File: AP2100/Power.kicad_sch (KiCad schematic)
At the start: 35 parts, among them U2 MPQ8634AGLE-P, U3 MPQ8634AGLE-P

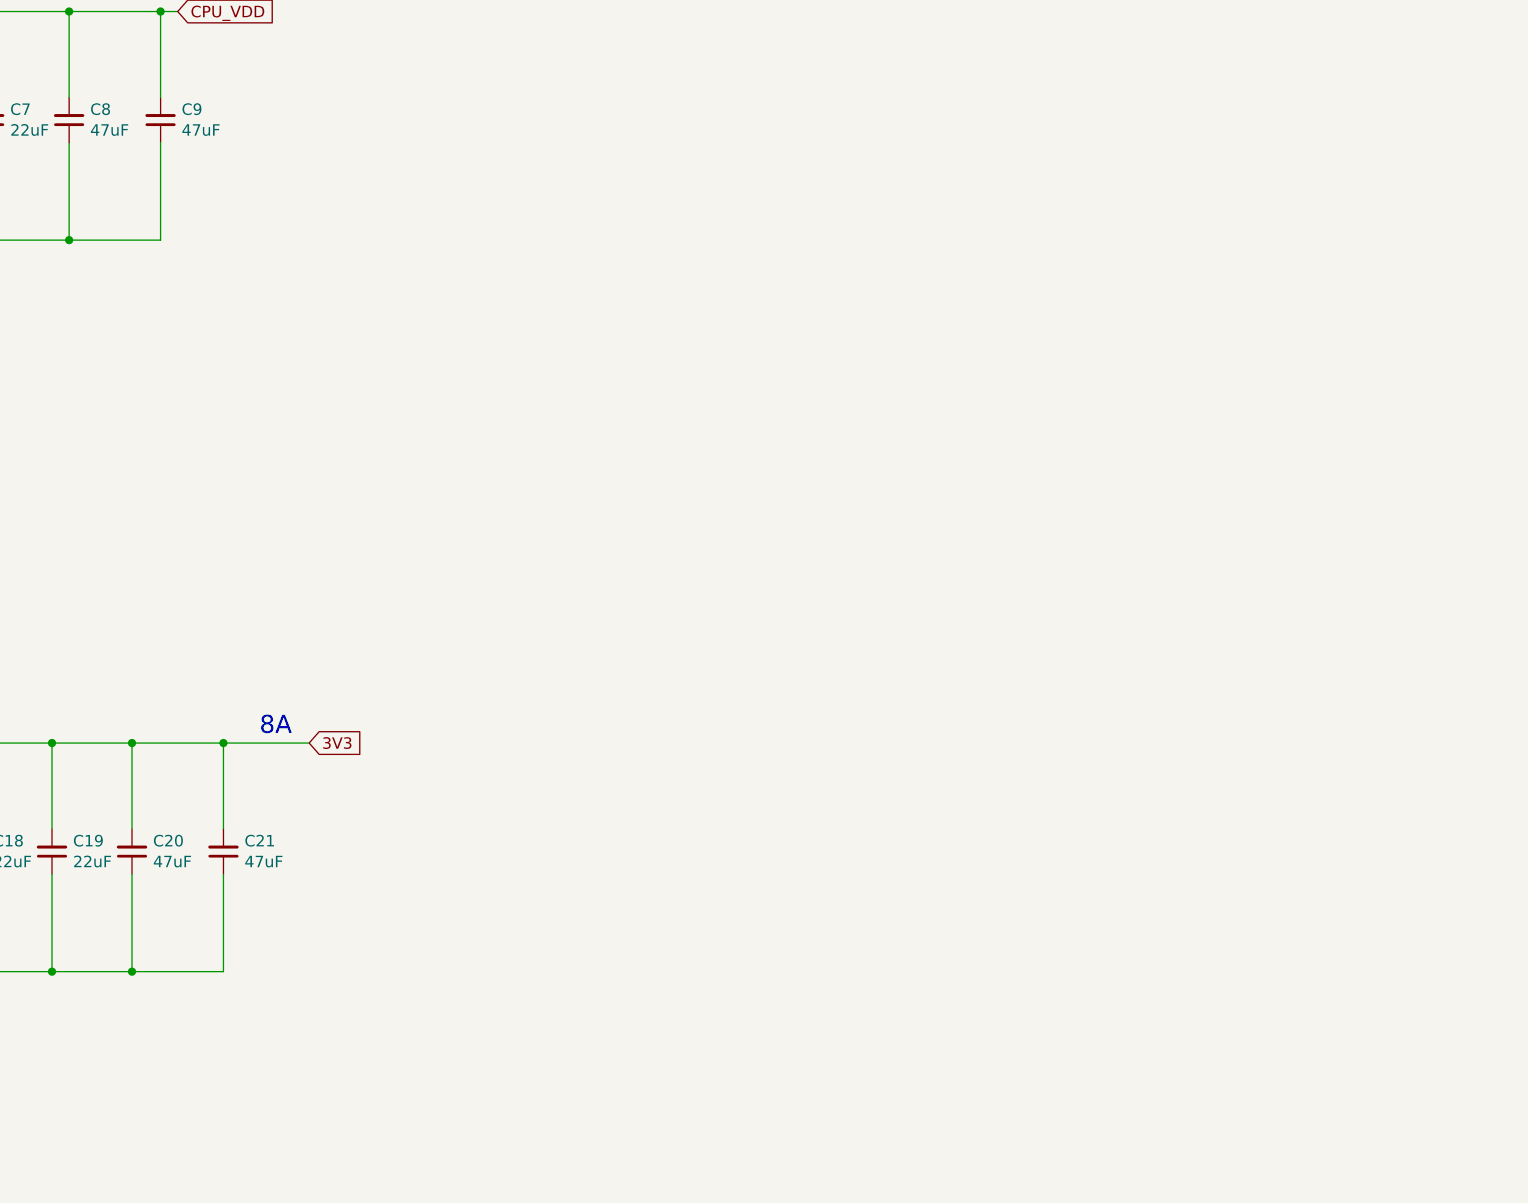
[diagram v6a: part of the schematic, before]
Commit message: Add 1.2V and 5V power supplies
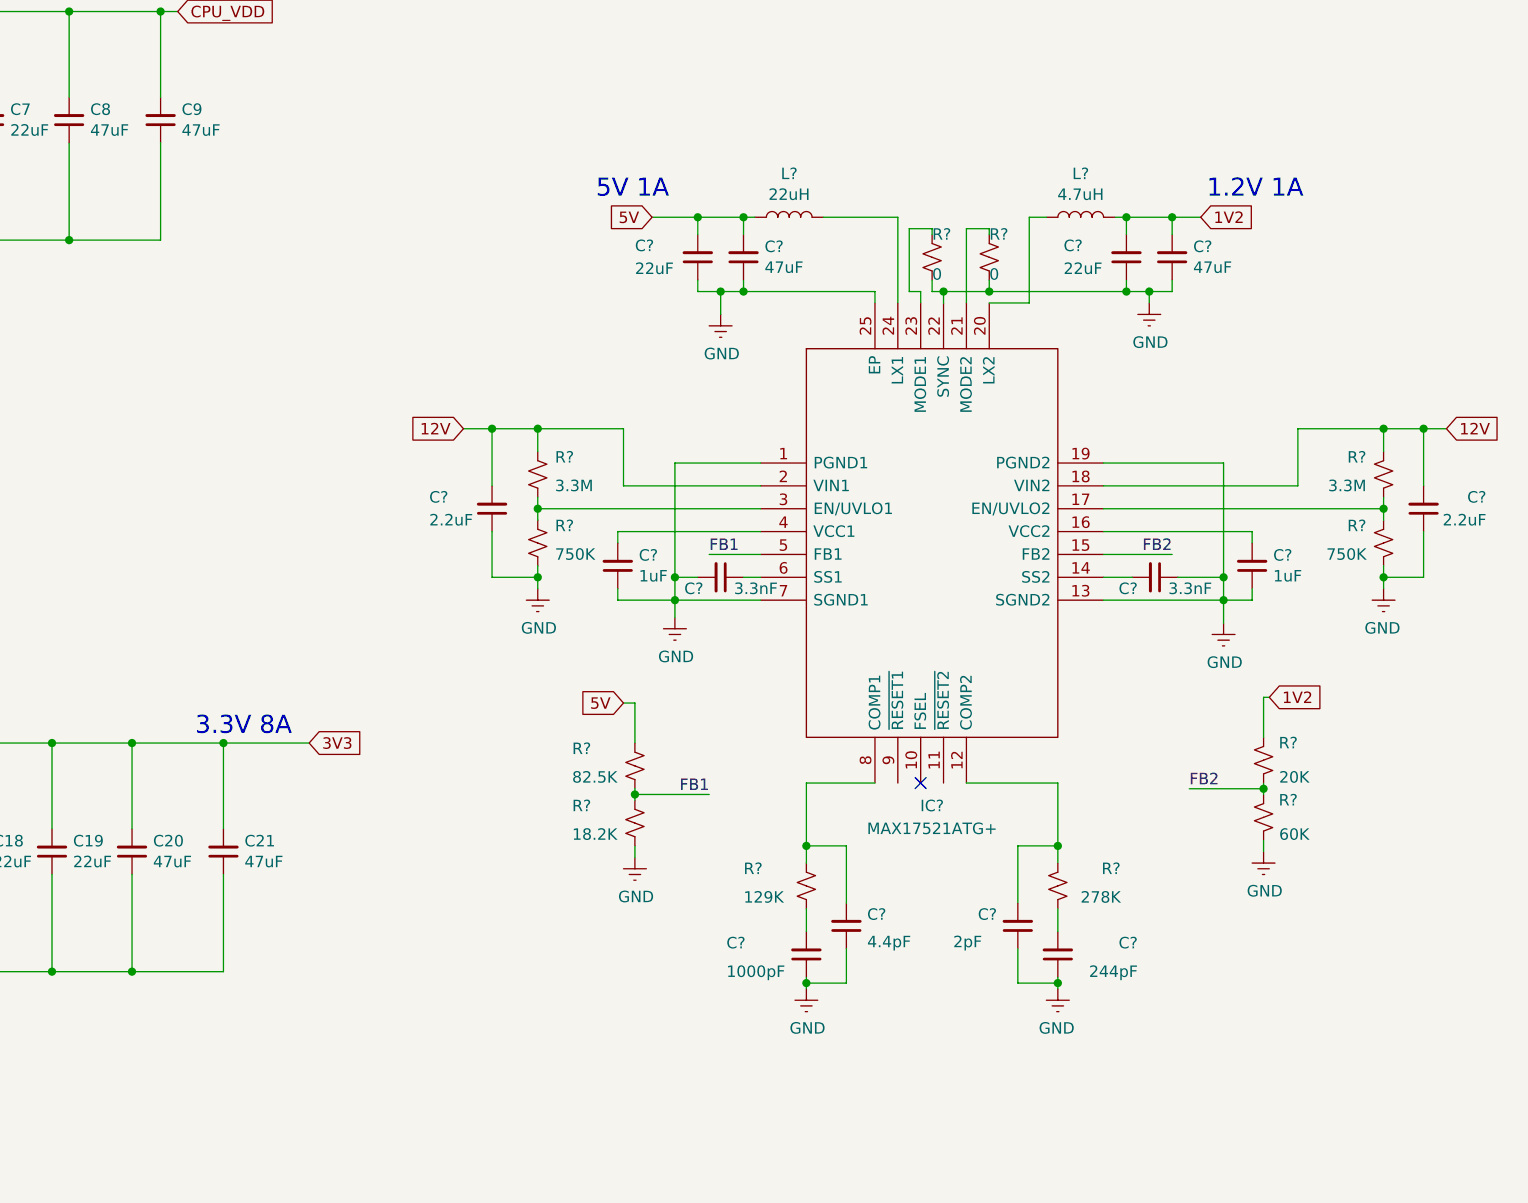
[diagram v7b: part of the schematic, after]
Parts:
- added C? (x2): 22uF, Capacitor_SMD:C_1210_3225Metric, symbol Device:C_Small
- added C? (x2): 1uF, Capacitor_SMD:C_0603_1608Metric, symbol Device:C_Small
- added C?: 244pF, Capacitor_SMD:C_0402_1005Metric, symbol Device:C_Small
- added C? (x2): 2.2uF, Capacitor_SMD:C_1210_3225Metric, symbol Device:C_Small
- added C?: 4.4pF, Capacitor_SMD:C_0402_1005Metric, symbol Device:C_Small
- added C? (x2): 47uF, Capacitor_SMD:C_1210_3225Metric, symbol Device:C_Small
- added C? (x2): 3.3nF, Capacitor_SMD:C_0402_1005Metric, symbol Device:C_Small
- added C?: 1000pF, Capacitor_SMD:C_0402_1005Metric, symbol Device:C_Small
- added C?: 2pF, Capacitor_SMD:C_0402_1005Metric, symbol Device:C_Small
- added IC?: MAX17521ATG+, QFN50P400X500X80-25N, symbol MAX17521ATG+:MAX17521ATG+
- added L?: 22uH, symbol Device:L
- added L?: 4.7uH, symbol Device:L
- added R? (x2): 0, Resistor_SMD:R_0402_1005Metric, symbol Device:R_Small_US
- added R?: 278K, Resistor_SMD:R_0402_1005Metric, symbol Device:R_Small_US
- added R? (x2): 3.3M, Resistor_SMD:R_0603_1608Metric, symbol Device:R_Small_US
- added R? (x2): 750K, Resistor_SMD:R_0603_1608Metric, symbol Device:R_Small_US
- added R?: 20K, Resistor_SMD:R_0402_1005Metric, symbol Device:R_Small_US
- added R?: 18.2K, Resistor_SMD:R_0402_1005Metric, symbol Device:R_Small_US
- added R?: 82.5K, Resistor_SMD:R_0402_1005Metric, symbol Device:R_Small_US
- added R?: 129K, Resistor_SMD:R_0402_1005Metric, symbol Device:R_Small_US
- added R?: 60K, Resistor_SMD:R_0402_1005Metric, symbol Device:R_Small_US
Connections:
- net 12V: now also C?.2, C?.2, IC?.18 (VIN2), IC?.2 (VIN1), R?.1, R?.1
- net GND: now also C?.1, C?.1, C?.1, C?.1, C?.1, C?.1, C?.1, C?.1, C?.1, C?.1, C?.1, C?.1, C?.1, C?.2, IC?.1 (PGND1), IC?.13 (SGND2), IC?.19 (PGND2), IC?.22 (SYNC), IC?.25 (EP), IC?.7 (SGND1), R?.2, R?.2, R?.2, R?.2, R?.2, R?.2
- new net: IC?.21 (MODE2), R?.1
- new net: C?.2, IC?.12 (COMP2), R?.1
- new net: C?.2, R?.2 (x2)
- new net: C?.2, IC?.4 (VCC1)
- new net: IC?.3 (EN/UVLO1), R?.1, R?.2
- new net: IC?.23 (MODE1), R?.1
- new net: IC?.17 (EN/UVLO2), R?.1, R?.2
- new net: IC?.24 (LX1), L?.2
- new net: C?.2, IC?.14 (SS2)
- new net: C?.2, IC?.16 (VCC2)
- new net: IC?.20 (LX2), L?.1
- new net: C?.1, IC?.6 (SS1)
- new net: C?.2, IC?.8 (COMP1), R?.1
- new net 1V2: C?.2, C?.2, L?.2, R?.1
- new net 5V: C?.2, C?.2, L?.1, R?.1
- new net FB1: IC?.5 (FB1), R?.1, R?.2
- new net FB2: IC?.15 (FB2), R?.1, R?.2
- no-connect marks 0 -> 1
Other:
- note added: "1.2V 1A"
- note added: "3.3V 8A"
- note added: "5V 1A"
- note removed: "8A"

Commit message: Add pmic chip to power section. Finish eMMC.
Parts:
- added C? (x8): .1uF, Capacitor_SMD:C_0402_1005Metric, symbol Device:C_Small
- added C? (x6): 1uF, Capacitor_SMD:C_0402_1005Metric, symbol Device:C_Small
- added C? (x14): 22uF, Capacitor_SMD:C_0805_2012Metric, symbol Device:C_Small
- added C? (x11): 4.7uF, Capacitor_SMD:C_0805_2012Metric, symbol Device:C_Small
- added C? (x3): 47uF, Capacitor_SMD:C_0603_1608Metric_Pad1.05x0.95mm_HandSolder, symbol Device:C_Small
- added C?: .47uF, Capacitor_SMD:C_0603_1608Metric, symbol Device:C_Small
- added C?: 500pF, Capacitor_SMD:C_0603_1608Metric, symbol Device:C_Small
- added C?: .22uF, Capacitor_SMD:C_0402_1005Metric, symbol Device:C_Small
- added L? (x3): 1.5uH, symbol Device:L
- added L?: 0.6uH, symbol Device:L
- added R?: 50K, Resistor_SMD:R_0402_1005Metric, symbol Device:R_Small_US
- added R?: 10K, Resistor_SMD:R_0603_1608Metric, symbol Device:R_Small_US
- added R?: 100K, Resistor_SMD:R_0402_1005Metric, symbol Device:R_Small_US
- added R? (x3): 10K, Resistor_SMD:R_0402_1005Metric, symbol Device:R_Small_US
- added R?: 499K, Resistor_SMD:R_0402_1005Metric, symbol Device:R_Small_US
- added R?: 90K, Resistor_SMD:R_0603_1608Metric, symbol Device:R_Small_US
- added U?: MC34VR500V4ES, QFN50P800X800X90-57N, symbol MC34VR500V4ES:MC34VR500V4ES
- C20, C21, C8, C9: value 47uF -> 100uF; PartsBoxID 1210-47uF-X5R-16V -> 1210-100uF-X5R-16V
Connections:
- net 12V: now also R?.2
- net 3V3: now also C?.2, C?.2, C?.2, C?.2, C?.2, C?.2, C?.2, C?.2, C?.2, C?.2, C?.2, C?.2, C?.2, C?.2, C?.2, C?.2, C?.2, R?.1, R?.2, U?.10 (PVIN1_2), U?.12 (PVIN1_3), U?.17 (VLDOIN1), U?.20 (PVIN4), U?.23 (PVIN2_1), U?.24 (PVIN2_2), U?.27 (VLDOIN23), U?.34 (PVIN3_1), U?.37 (PVIN3_2), U?.40 (VLDOIN45), U?.50 (VIN), U?.55 (VCCI2C), U?.7 (PVIN1_1)
- net CPU_VDD: now also C?.1, R?.2; no longer U2.7 (FB)
- net EN_VDD: now also C?.2, R?.1, U?.26 (LDO2); no longer U2.8 (EN)
- net GND: now also C?.1, C?.1, C?.1, C?.1, C?.1, C?.1, C?.1, C?.1, C?.1, C?.1, C?.1, C?.1, C?.1, C?.1, C?.1, C?.1, C?.1, C?.1, C?.1, C?.1, C?.1, C?.1, C?.1, C?.1, C?.1, C?.1, C?.1, C?.1, C?.1, C?.1, C?.1, C?.1, C?.1, C?.1, C?.1, C?.1, C?.1, C?.1, C?.1, C?.1, C?.1, C?.1, C?.1, R?.1, R?.1, R?.1, U?.14 (SGND1), U?.15 (SGND2), U?.32 (SGND3), U?.47 (ICTEST2), U?.48 (SGND4), U?.5 (ICTEST1), U?.57 (EP)
- net EN_3V3: no longer names the net of U3.8 (EN)
- net EN_3V3: now also R?.1, R?.2
- new net: C?.2, R?.1, R?.2, U2.7 (FB)
- new net: R?.2, U2.8 (EN)
- new net: C?.2, C?.2, U?.29 (VHALF)
- new net: L?.2, U?.35 (LX3_1), U?.36 (LX3_2)
- new net: L?.2, U?.11 (LX1_3), U?.8 (LX1_1), U?.9 (LX1_2)
- new net: C?.2, U?.43 (VBIAS)
- new net: C?.2, U?.52 (VBG)
- new net: C?.2, U?.51 (VDIG)
- new net: C?.2, U?.49 (VCC)
- new net: R?.2, U?.56 (EN)
- new net: U?.16 (NC), U?.2 (NC), U?.33 (NC), U?.42 (NC), U?.44 (NC), U?.45 (NC), U?.46 (NC), U?.6 (NC)
- new net: L?.2, U?.21 (LX4)
- new net: L?.2, U?.22 (LX2)
- new net: R?.2, U?.4 (STBY)
- new net 1V5: C?.2, C?.2, C?.2, C?.2, C?.2, C?.2, L?.1, U?.13 (FB1)
- new net 1V8: C?.2, C?.2, L?.1, U?.25 (FB2)
- new net 2V5_VPP: C?.2, U?.28 (LDO3)
- new net BAKUP1: C?.2, U?.39 (LDO4)
- new net BAKUP2: C?.2, U?.41 (LDO5)
- new net DDR_VREF: C?.2, U?.31 (REFOUT)
- new net DDR_VTT: C?.2, C?.2, L?.1, U?.19 (FB4)
- new net GVDD: C?.1, C?.2, C?.2, C?.2, C?.2, C?.2, L?.1, U?.30 (REFIN), U?.38 (FB3)
- new net I2C1_SCL: U?.54 (SCL)
- new net I2C1_SDA: U?.53 (SDA)
- new net PMIC_INT_B: R?.1, U?.1 (~INT~)
- new net PMIC_POR_B: U?.3 (~POR~)
- new net PWR_X1VDD: C?.2, U?.18 (LDO1)
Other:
- note added: "0.6V 1A"
- note added: "1.0V 8A"
- note added: "1.2V 2.5A"
- note added: "1.35V"
- note added: "1.5V 4.5A"
- note added: "1.8V"
- note added: "1.8V 2A"
- note added: "100mA"
- note added: "2.5V"
- note added: "200mA"
- note added: "250mA"
- note added: "3.3V"
- note added: "350mA"
- note removed: "0.9V 8A"
- moved on the sheet: C1, C10, C11, C12, C13, C14, C15, C16, C17, C18, C19, C2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
